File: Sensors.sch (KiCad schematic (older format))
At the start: 16 parts, among them U4 MPRLS0015PA0000SA, U5 MPRLS0015PA0000SA

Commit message: Review update
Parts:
- removed CONN8: Digital input 2, Molex Picoblade 2 pin, symbol actuator-board-rescue:CONN_2PIN-_connectors
- CONN5: value ADC_2PIN, Molex Picoblade 2 pin -> ANALOG2
- CONN6: value ADC_2PIN, Molex Picoblade 2 pin -> ANALOG1
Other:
- note added: "Input range = 0-6.6V\nFc = 318 Hz\n(10k+10k)/(10k*10k*100nF*2*pi)"
- note added: "Notes:\n- Absolute pressure\n- 0 - 1 atm\n- SPI mode\n- output range: 24bits 10%-90%"
- note removed: "Fc = 318 Hz\n(10k+10k)/(10k*10k*100nF*2*pi)"
- moved on the sheet: C12, CONN5, CONN7, R10, R9
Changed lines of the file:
@@
 Sheet 2 3
 Title "Actuator board"
-Date "2020-01-18"
-Rev "A"
+Date "2020-02-12"
+Rev "A.4"
 Comp "Club Vaudois de Robotique Autonome"
 Comment1 "Salah Missri"
@@
 Text HLabel 3350 4350 0    50   Input ~ 0
 ANALOG_SENS_IN1
-Text HLabel 3350 5125 0    50   Input ~ 0
+Text HLabel 3350 5150 0    50   Input ~ 0
 ANALOG_SENS_IN2
-$Comp
-L _connectors:ADC_2PIN CONN5
-U 1 1 5E2563B4
-P 4375 5725
-F 0 "CONN5" H 4553 6128 59  0000 L CNN
-F 1 "ADC_2PIN, Molex Picoblade 2 pin" H 4553 6023 59  0000 L CNN
-F 2 "" H 4375 5725 59  0001 C CNN
-F 3 "" H 4375 5725 59  0000 C CNN
-	1    4375 5725
-	1    0    0    -1
-$EndComp
-Text HLabel 7450 4750 0    50   Input ~ 0
+Text HLabel 7300 4550 0    50   Input ~ 0
 DIGITAL_IN1
-$Comp
-L actuator-board-rescue:CONN_2PIN-_connectors CONN?
-U 1 1 5E2B70AE
-P 7800 5600
-AR Path="/5E2B70AE" Ref="CONN?"  Part="1"
-AR Path="/5E1FAFCF/5E2B70AE" Ref="CONN8"  Part="1"
-F 0 "CONN8" H 8018 6003 59  0000 L CNN
-F 1 "Digital input 2, Molex Picoblade 2 pin" H 8018 5898 59  0000 L CNN
-F 2 "" H 7800 5600 59  0001 C CNN
-F 3 "" H 7800 5600 59  0000 C CNN
-	1    7800 5600
-	1    0    0    -1
-$EndComp
-Text HLabel 7450 5200 0    50   Input ~ 0
-DIGITAL_IN2
 Text HLabel 6950 3200 0    50   Input ~ 0
 VACUUM_SENS2_RESET
@@
 L actuator-board-rescue:CONN_2PIN-_connectors CONN?
 U 1 1 5E2B60FB
-P 7800 5150
+P 7650 4950
 AR Path="/5E2B60FB" Ref="CONN?"  Part="1"
 AR Path="/5E1FAFCF/5E2B60FB" Ref="CONN7"  Part="1"
-F 0 "CONN7" H 8018 5553 59  0000 L CNN
-F 1 "Digital input 1, Molex Picoblade 2 pin" H 8018 5448 59  0000 L CNN
-F 2 "" H 7800 5150 59  0001 C CNN
-F 3 "" H 7800 5150 59  0000 C CNN
-	1    7800 5150
+F 0 "CONN7" H 7868 5353 59  0000 L CNN
+F 1 "Digital input 1, Molex Picoblade 2 pin" H 7868 5248 59  0000 L CNN
+F 2 "" H 7650 4950 59  0001 C CNN
+F 3 "" H 7650 4950 59  0000 C CNN
+	1    7650 4950
 	1    0    0    -1
 $EndComp
@@
 Wire Wire Line
 	3400 4650 3650 4650
-Text Notes 2325 4550 0    39   ~ 0
-Fc = 318 Hz\n(10k+10k)/(10k*10k*100nF*2*pi)
 Wire Wire Line
 	3350 4350 3400 4350
 Connection ~ 3400 4350
-Text Notes 2325 5325 0    39   ~ 0
-Fc = 318 Hz\n(10k+10k)/(10k*10k*100nF*2*pi)
 $Comp
 L Device:R_Small R9
 U 1 1 5E315BC9
-P 3675 4975
-F 0 "R9" H 3734 5013 39  0000 L CNN
-F 1 "10k" H 3734 4938 39  0000 L CNN
-F 2 "" H 3675 4975 50  0001 C CNN
-F 3 "~" H 3675 4975 50  0001 C CNN
-	1    3675 4975
+P 3675 5000
+F 0 "R9" H 3734 5038 39  0000 L CNN
+F 1 "10k" H 3734 4963 39  0000 L CNN
+F 2 "" H 3675 5000 50  0001 C CNN
+F 3 "~" H 3675 5000 50  0001 C CNN
+	1    3675 5000
 	1    0    0    -1
 $EndComp
@@
 L Device:C_Small C12
 U 1 1 5E315BCA
-P 3400 5275
-F 0 "C12" H 3450 5325 39  0000 L CNN
-F 1 "0.1uF" H 3450 5225 39  0000 L CNN
-F 2 "Capacitor_SMD:C_0603_1608Metric" H 3400 5275 50  0001 C CNN
-F 3 "~" H 3400 5275 50  0001 C CNN
-	1    3400 5275
+P 3400 5300
+F 0 "C12" H 3450 5350 39  0000 L CNN
+F 1 "0.1uF" H 3450 5250 39  0000 L CNN
+F 2 "Capacitor_SMD:C_0603_1608Metric" H 3400 5300 50  0001 C CNN
+F 3 "~" H 3400 5300 50  0001 C CNN
+	1    3400 5300
 	1    0    0    -1
 $EndComp
@@
 L Device:R_Small R10
 U 1 1 5E315BCB
-P 3675 5275
-F 0 "R10" H 3734 5313 39  0000 L CNN
-F 1 "10k" H 3734 5238 39  0000 L CNN
-F 2 "" H 3675 5275 50  0001 C CNN
-F 3 "~" H 3675 5275 50  0001 C CNN
-	1    3675 5275
+P 3675 5300
+F 0 "R10" H 3734 5338 39  0000 L CNN
+F 1 "10k" H 3734 5263 39  0000 L CNN
+F 2 "" H 3675 5300 50  0001 C CNN
+F 3 "~" H 3675 5300 50  0001 C CNN
+	1    3675 5300
 	1    0    0    -1
 $EndComp
@@
 P 4400 4950
 F 0 "CONN6" H 4578 5353 59  0000 L CNN
-F 1 "ADC_2PIN, Molex Picoblade 2 pin" H 4578 5248 59  0000 L CNN
+F 1 "ANALOG1" H 4578 5248 59  0000 L CNN
 F 2 "" H 4400 4950 59  0001 C CNN
 F 3 "" H 4400 4950 59  0000 C CNN
@@
 $EndComp
 Wire Wire Line
-	3875 4550 4050 4550
-Wire Wire Line
-	3675 4875 3875 4875
-Wire Wire Line
-	3875 4875 3875 5325
-Wire Wire Line
-	3875 5325 4025 5325
-Wire Wire Line
-	3400 5425 3675 5425
-Wire Wire Line
-	3675 5075 3675 5125
-Wire Wire Line
-	3350 5125 3400 5125
-Connection ~ 3400 5125
-Wire Wire Line
-	3400 5125 3675 5125
+	3900 4550 4050 4550
+Wire Wire Line
+	3675 4900 3900 4900
+Wire Wire Line
+	3900 4900 3900 5350
+Wire Wire Line
+	3400 5450 3675 5450
+Wire Wire Line
+	3675 5100 3675 5150
+Wire Wire Line
+	3350 5150 3400 5150
+Connection ~ 3400 5150
+Wire Wire Line
+	3400 5150 3675 5150
 $Comp
 L power:VCC #PWR025
@@
 L power:GND #PWR029
 U 1 1 5E4F62EA
-P 7450 4850
-F 0 "#PWR029" H 7450 4600 50  0001 C CNN
-F 1 "GND" H 7455 4677 50  0000 C CNN
-F 2 "" H 7450 4850 50  0001 C CNN
-F 3 "" H 7450 4850 50  0001 C CNN
-	1    7450 4850
-	1    0    0    -1
-$EndComp
-$Comp
-L power:GND #PWR030
-U 1 1 5E4F6F64
-P 7450 5300
-F 0 "#PWR030" H 7450 5050 50  0001 C CNN
-F 1 "GND" H 7455 5127 50  0000 C CNN
-F 2 "" H 7450 5300 50  0001 C CNN
-F 3 "" H 7450 5300 50  0001 C CNN
-	1    7450 5300
+P 7300 4650
+F 0 "#PWR029" H 7300 4400 50  0001 C CNN
+F 1 "GND" H 7305 4477 50  0000 C CNN
+F 2 "" H 7300 4650 50  0001 C CNN
+F 3 "" H 7300 4650 50  0001 C CNN
+	1    7300 4650
 	1    0    0    -1
 $EndComp
@@
 	3650 4650 4050 4650
 Wire Wire Line
-	4025 5425 3675 5425
-Connection ~ 3675 5425
+	4050 5450 3675 5450
+Connection ~ 3675 5450
 $Comp
 L power:GND #PWR024
 U 1 1 5E503BBC
-P 3675 5425
-F 0 "#PWR024" H 3675 5175 50  0001 C CNN
-F 1 "GND" H 3680 5252 50  0000 C CNN
-F 2 "" H 3675 5425 50  0001 C CNN
-F 3 "" H 3675 5425 50  0001 C CNN
-	1    3675 5425
-	1    0    0    -1
-$EndComp
-Wire Wire Line
-	3875 4100 3875 4550
+P 3675 5450
+F 0 "#PWR024" H 3675 5200 50  0001 C CNN
+F 1 "GND" H 3680 5277 50  0000 C CNN
+F 2 "" H 3675 5450 50  0001 C CNN
+F 3 "" H 3675 5450 50  0001 C CNN
+	1    3675 5450
+	1    0    0    -1
+$EndComp
+Wire Wire Line
+	3900 4100 3900 4550
 Wire Wire Line
 	3650 4300 3650 4350
 Wire Wire Line
-	3875 4100 3650 4100
+	3900 4100 3650 4100
 $Comp
 L Device:R_Small R7
@@
 $EndComp
 Wire Wire Line
-	3400 5125 3400 5175
-Wire Wire Line
-	3400 5375 3400 5425
-Connection ~ 3675 5125
-Wire Wire Line
-	3675 5125 3675 5175
-Wire Wire Line
-	3675 5375 3675 5425
+	3400 5150 3400 5200
+Wire Wire Line
+	3400 5400 3400 5450
+Connection ~ 3675 5150
+Wire Wire Line
+	3675 5150 3675 5200
+Wire Wire Line
+	3675 5400 3675 5450
 Text HLabel 3500 2600 0    50   Input ~ 0
 SPI_SCK
@@
 	1    0    0    -1
 $EndComp
+$Comp
+L _connectors:ADC_2PIN CONN5
+U 1 1 5E2563B4
+P 4400 5750
+F 0 "CONN5" H 4578 6153 59  0000 L CNN
+F 1 "ANALOG2" H 4578 6048 59  0000 L CNN
+F 2 "" H 4400 5750 59  0001 C CNN
+F 3 "" H 4400 5750 59  0000 C CNN
+	1    4400 5750
+	1    0    0    -1
+$EndComp
+Wire Wire Line
+	3900 5350 4050 5350
+Text Notes 2400 2150 0    50   ~ 0
+Notes:\n- Absolute pressure\n- 0 - 1 atm\n- SPI mode\n- output range: 24bits 10%-90%
+Text Notes 5250 5100 0    50   ~ 0
+Input range = 0-6.6V\nFc = 318 Hz\n(10k+10k)/(10k*10k*100nF*2*pi)
+Wire Notes Line
+	5050 5600 5150 5600
+Wire Notes Line
+	5150 5600 5150 4400
+Wire Notes Line
+	5150 4400 5050 4400
 $EndSCHEMATC

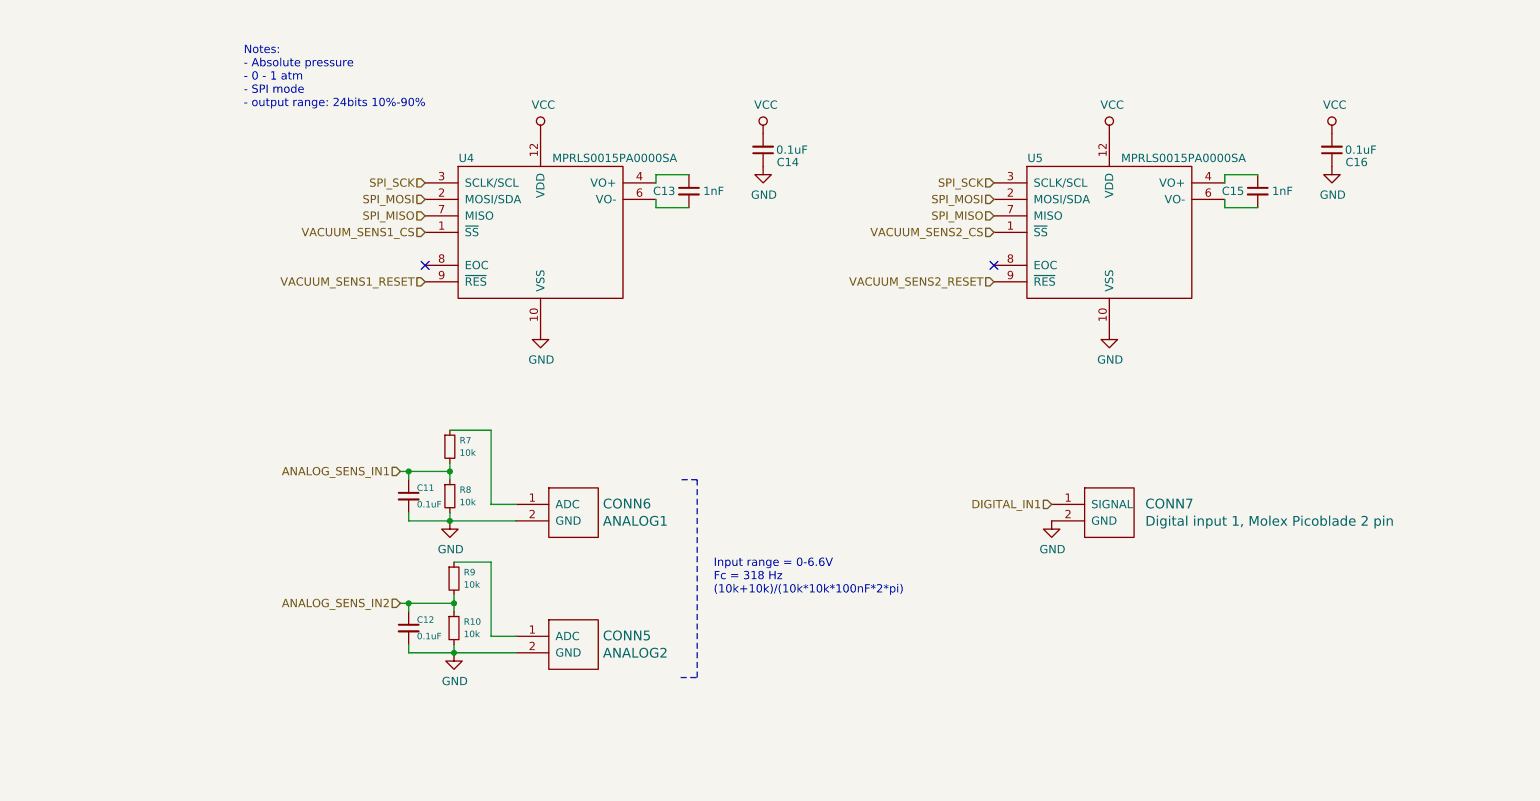
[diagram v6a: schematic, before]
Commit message: Input range note, rough footprint assignment
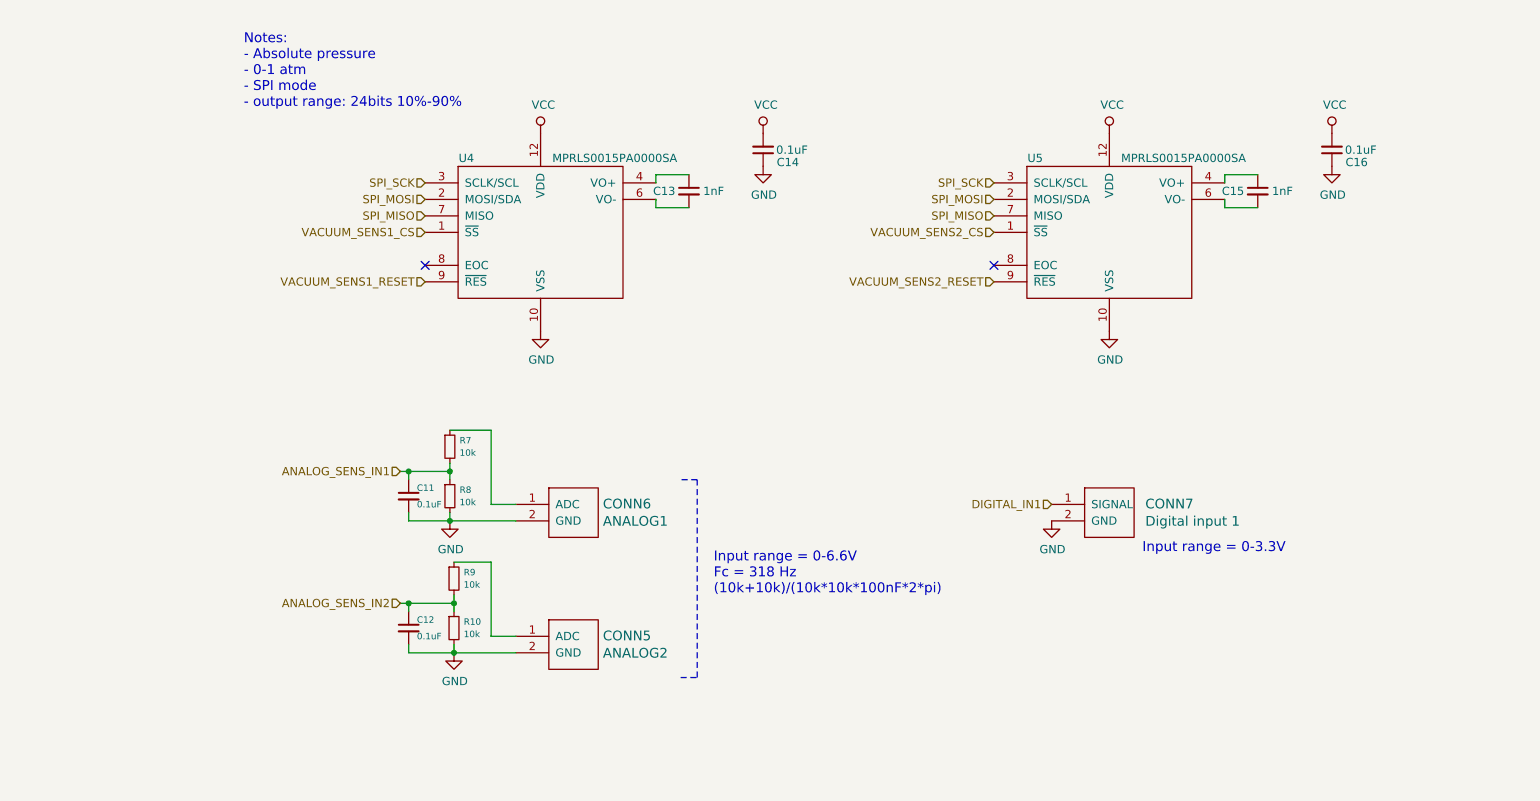
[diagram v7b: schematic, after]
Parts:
- CONN5, CONN6: footprint (none) -> Connector_Molex:Molex_PicoBlade_53261-0271_1x02-1MP_P1.25mm_Horizontal
- CONN7: value Digital input 1, Molex Picoblade 2 pin -> Digital input 1; footprint (none) -> Connector_Molex:Molex_PicoBlade_53261-0271_1x02-1MP_P1.25mm_Horizontal
- R10, R7, R8, R9: footprint (none) -> Resistor_SMD:R_0603_1608Metric
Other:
- note added: "Input range = 0-3.3V"
- note added: "Notes:\n- Absolute pressure\n- 0-1 atm\n- SPI mode\n- output range: 24bits 10%-90%"
- note removed: "Notes:\n- Absolute pressure\n- 0 - 1 atm\n- SPI mode\n- output range: 24bits 10%-90%"
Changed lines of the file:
@@
 AR Path="/5E1FAFCF/5E2B60FB" Ref="CONN7"  Part="1"
 F 0 "CONN7" H 7868 5353 59  0000 L CNN
-F 1 "Digital input 1, Molex Picoblade 2 pin" H 7868 5248 59  0000 L CNN
-F 2 "" H 7650 4950 59  0001 C CNN
+F 1 "Digital input 1" H 7868 5248 59  0000 L CNN
+F 2 "Connector_Molex:Molex_PicoBlade_53261-0271_1x02-1MP_P1.25mm_Horizontal" H 7650 4950 59  0001 C CNN
 F 3 "" H 7650 4950 59  0000 C CNN
 	1    7650 4950
@@
 F 0 "R9" H 3734 5038 39  0000 L CNN
 F 1 "10k" H 3734 4963 39  0000 L CNN
-F 2 "" H 3675 5000 50  0001 C CNN
+F 2 "Resistor_SMD:R_0603_1608Metric" H 3675 5000 50  0001 C CNN
 F 3 "~" H 3675 5000 50  0001 C CNN
 	1    3675 5000
@@
 F 0 "R10" H 3734 5338 39  0000 L CNN
 F 1 "10k" H 3734 5263 39  0000 L CNN
-F 2 "" H 3675 5300 50  0001 C CNN
+F 2 "Resistor_SMD:R_0603_1608Metric" H 3675 5300 50  0001 C CNN
 F 3 "~" H 3675 5300 50  0001 C CNN
 	1    3675 5300
@@
 F 0 "CONN6" H 4578 5353 59  0000 L CNN
 F 1 "ANALOG1" H 4578 5248 59  0000 L CNN
-F 2 "" H 4400 4950 59  0001 C CNN
+F 2 "Connector_Molex:Molex_PicoBlade_53261-0271_1x02-1MP_P1.25mm_Horizontal" H 4400 4950 59  0001 C CNN
 F 3 "" H 4400 4950 59  0000 C CNN
 	1    4400 4950
@@
 F 0 "R7" H 3709 4238 39  0000 L CNN
 F 1 "10k" H 3709 4163 39  0000 L CNN
-F 2 "" H 3650 4200 50  0001 C CNN
+F 2 "Resistor_SMD:R_0603_1608Metric" H 3650 4200 50  0001 C CNN
 F 3 "~" H 3650 4200 50  0001 C CNN
 	1    3650 4200
@@
 F 0 "R8" H 3709 4538 39  0000 L CNN
 F 1 "10k" H 3709 4463 39  0000 L CNN
-F 2 "" H 3650 4500 50  0001 C CNN
+F 2 "Resistor_SMD:R_0603_1608Metric" H 3650 4500 50  0001 C CNN
 F 3 "~" H 3650 4500 50  0001 C CNN
 	1    3650 4500
@@
 F 0 "CONN5" H 4578 6153 59  0000 L CNN
 F 1 "ANALOG2" H 4578 6048 59  0000 L CNN
-F 2 "" H 4400 5750 59  0001 C CNN
+F 2 "Connector_Molex:Molex_PicoBlade_53261-0271_1x02-1MP_P1.25mm_Horizontal" H 4400 5750 59  0001 C CNN
 F 3 "" H 4400 5750 59  0000 C CNN
 	1    4400 5750
@@
 Wire Wire Line
 	3900 5350 4050 5350
-Text Notes 2400 2150 0    50   ~ 0
-Notes:\n- Absolute pressure\n- 0 - 1 atm\n- SPI mode\n- output range: 24bits 10%-90%
-Text Notes 5250 5100 0    50   ~ 0
+Text Notes 2400 2150 0    60   ~ 0
+Notes:\n- Absolute pressure\n- 0-1 atm\n- SPI mode\n- output range: 24bits 10%-90%
+Text Notes 5250 5100 0    60   ~ 0
 Input range = 0-6.6V\nFc = 318 Hz\n(10k+10k)/(10k*10k*100nF*2*pi)
 Wire Notes Line
@@
 Wire Notes Line
 	5150 4400 5050 4400
+Text Notes 7850 4850 0    60   ~ 0
+Input range = 0-3.3V
 $EndSCHEMATC

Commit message: Upadate footprints, rough arrangement
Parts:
- removed CONN5: ANALOG2, Connector_Molex:Molex_PicoBlade_53261-0271_1x02-1MP_P1.25mm_Horizontal, symbol _connectors:ADC_2PIN
- removed CONN6: ANALOG1, Connector_Molex:Molex_PicoBlade_53261-0271_1x02-1MP_P1.25mm_Horizontal, symbol _connectors:ADC_2PIN
- removed CONN7: Digital input 1, Connector_Molex:Molex_PicoBlade_53261-0271_1x02-1MP_P1.25mm_Horizontal, symbol actuator-board-rescue:CONN_2PIN-_connectors
- added J2: Conn_01x06, Connector_Molex:Molex_PicoBlade_53261-0671_1x06-1MP_P1.25mm_Horizontal, symbol Connector_Generic:Conn_01x06
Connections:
- net DIGITAL_IN1: now also J2.5 (Pin_5)
- net GND: now also J2.2 (Pin_2), J2.4 (Pin_4), J2.6 (Pin_6)
- net at R7.1: now also J2.1 (Pin_1)
- net at R9.1: now also J2.3 (Pin_3)
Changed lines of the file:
@@
 Text HLabel 3350 5150 0    50   Input ~ 0
 ANALOG_SENS_IN2
-Text HLabel 7300 4550 0    50   Input ~ 0
+Text HLabel 4050 6050 0    50   Input ~ 0
 DIGITAL_IN1
 Text HLabel 6950 3200 0    50   Input ~ 0
 VACUUM_SENS2_RESET
-$Comp
-L actuator-board-rescue:CONN_2PIN-_connectors CONN?
-U 1 1 5E2B60FB
-P 7650 4950
-AR Path="/5E2B60FB" Ref="CONN?"  Part="1"
-AR Path="/5E1FAFCF/5E2B60FB" Ref="CONN7"  Part="1"
-F 0 "CONN7" H 7868 5353 59  0000 L CNN
-F 1 "Digital input 1" H 7868 5248 59  0000 L CNN
-F 2 "Connector_Molex:Molex_PicoBlade_53261-0271_1x02-1MP_P1.25mm_Horizontal" H 7650 4950 59  0001 C CNN
-F 3 "" H 7650 4950 59  0000 C CNN
-	1    7650 4950
-	1    0    0    -1
-$EndComp
 $Comp
 L Device:C_Small C11
@@
 	1    0    0    -1
 $EndComp
-$Comp
-L _connectors:ADC_2PIN CONN6
-U 1 1 5E255B96
-P 4400 4950
-F 0 "CONN6" H 4578 5353 59  0000 L CNN
-F 1 "ANALOG1" H 4578 5248 59  0000 L CNN
-F 2 "Connector_Molex:Molex_PicoBlade_53261-0271_1x02-1MP_P1.25mm_Horizontal" H 4400 4950 59  0001 C CNN
-F 3 "" H 4400 4950 59  0000 C CNN
-	1    4400 4950
-	1    0    0    -1
-$EndComp
-Wire Wire Line
-	3900 4550 4050 4550
+Wire Wire Line
+	3900 4550 4350 4550
 Wire Wire Line
 	3675 4900 3900 4900
@@
 L power:GND #PWR029
 U 1 1 5E4F62EA
-P 7300 4650
-F 0 "#PWR029" H 7300 4400 50  0001 C CNN
-F 1 "GND" H 7305 4477 50  0000 C CNN
-F 2 "" H 7300 4650 50  0001 C CNN
-F 3 "" H 7300 4650 50  0001 C CNN
-	1    7300 4650
+P 4350 5050
+F 0 "#PWR029" H 4350 4800 50  0001 C CNN
+F 1 "GND" H 4355 4877 50  0000 C CNN
+F 2 "" H 4350 5050 50  0001 C CNN
+F 3 "" H 4350 5050 50  0001 C CNN
+	1    4350 5050
 	1    0    0    -1
 $EndComp
@@
 Connection ~ 3650 4650
 Wire Wire Line
-	3650 4650 4050 4650
-Wire Wire Line
-	4050 5450 3675 5450
+	3650 4650 4350 4650
 Connection ~ 3675 5450
 $Comp
@@
 	1    0    0    -1
 $EndComp
-$Comp
-L _connectors:ADC_2PIN CONN5
-U 1 1 5E2563B4
-P 4400 5750
-F 0 "CONN5" H 4578 6153 59  0000 L CNN
-F 1 "ANALOG2" H 4578 6048 59  0000 L CNN
-F 2 "Connector_Molex:Molex_PicoBlade_53261-0271_1x02-1MP_P1.25mm_Horizontal" H 4400 5750 59  0001 C CNN
-F 3 "" H 4400 5750 59  0000 C CNN
-	1    4400 5750
-	1    0    0    -1
-$EndComp
 Wire Wire Line
 	3900 5350 4050 5350
 Text Notes 2400 2150 0    60   ~ 0
 Notes:\n- Absolute pressure\n- 0-1 atm\n- SPI mode\n- output range: 24bits 10%-90%
-Text Notes 5250 5100 0    60   ~ 0
+Text Notes 1000 5000 0    60   ~ 0
 Input range = 0-6.6V\nFc = 318 Hz\n(10k+10k)/(10k*10k*100nF*2*pi)
 Wire Notes Line
-	5050 5600 5150 5600
+	2250 5600 2350 5600
 Wire Notes Line
-	5150 5600 5150 4400
+	2350 5600 2350 4400
 Wire Notes Line
-	5150 4400 5050 4400
-Text Notes 7850 4850 0    60   ~ 0
+	2350 4400 2250 4400
+Text Notes 1450 6250 0    60   ~ 0
 Input range = 0-3.3V
+$Comp
+L Connector_Generic:Conn_01x06 J2
+U 1 1 5E47357A
+P 4550 4750
+F 0 "J2" H 4630 4742 50  0000 L CNN
+F 1 "Conn_01x06" H 4630 4651 50  0000 L CNN
+F 2 "Connector_Molex:Molex_PicoBlade_53261-0671_1x06-1MP_P1.25mm_Horizontal" H 4550 4750 50  0001 C CNN
+F 3 "~" H 4550 4750 50  0001 C CNN
+	1    4550 4750
+	1    0    0    -1
+$EndComp
+Wire Wire Line
+	4050 5350 4050 4750
+Wire Wire Line
+	4050 4750 4350 4750
+Wire Wire Line
+	4150 5450 4150 4850
+Wire Wire Line
+	4150 4850 4350 4850
+Wire Wire Line
+	3675 5450 4150 5450
+Wire Wire Line
+	4350 4950 4250 4950
+Wire Wire Line
+	4250 4950 4250 6050
+Wire Wire Line
+	4250 6050 4050 6050
 $EndSCHEMATC
